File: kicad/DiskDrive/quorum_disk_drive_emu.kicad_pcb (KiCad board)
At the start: 2 copper layers, 185 x 115 mm, 89 parts, among them X1 CONN_28, X103 CONN_28, X104 CONN_28, X2 CONN_28, X3 FDD, X4 FDD POWER

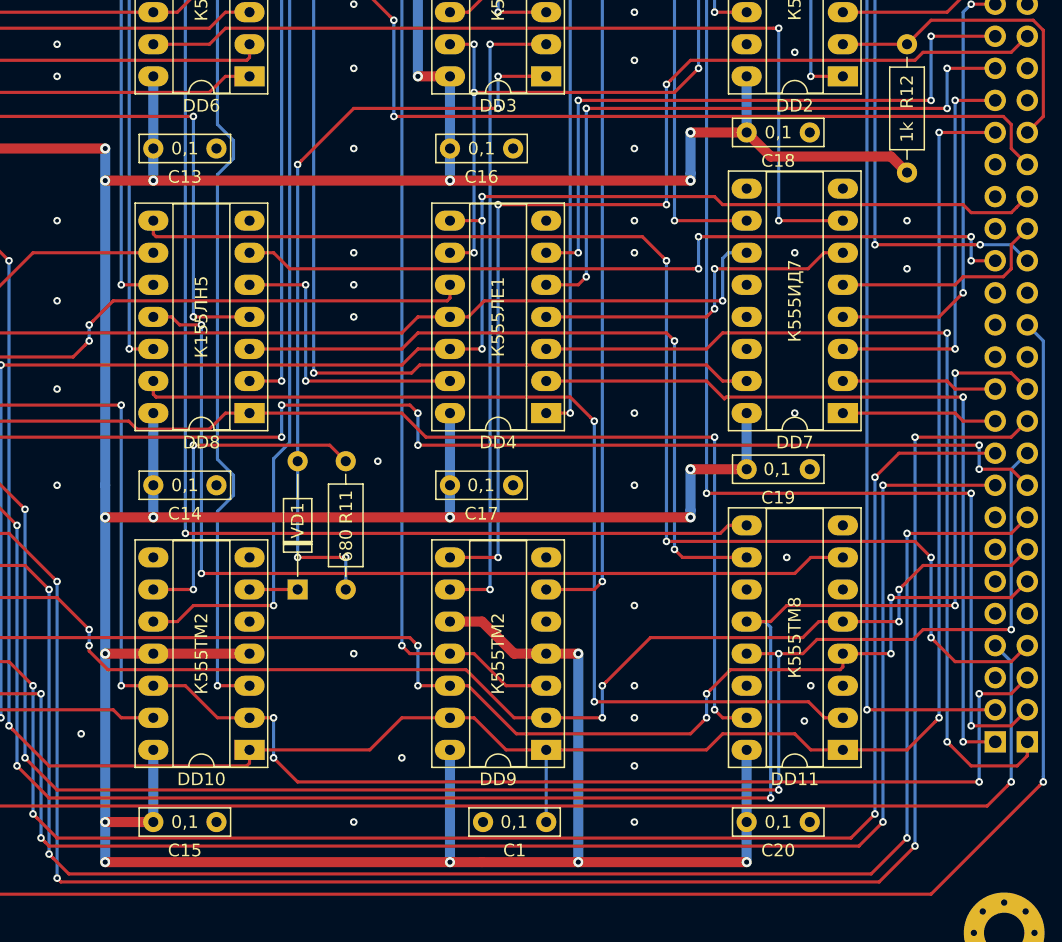
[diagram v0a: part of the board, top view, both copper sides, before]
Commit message: Обновлены УГО разъемов, исправлены множественные ошибки в схемах клавиатур
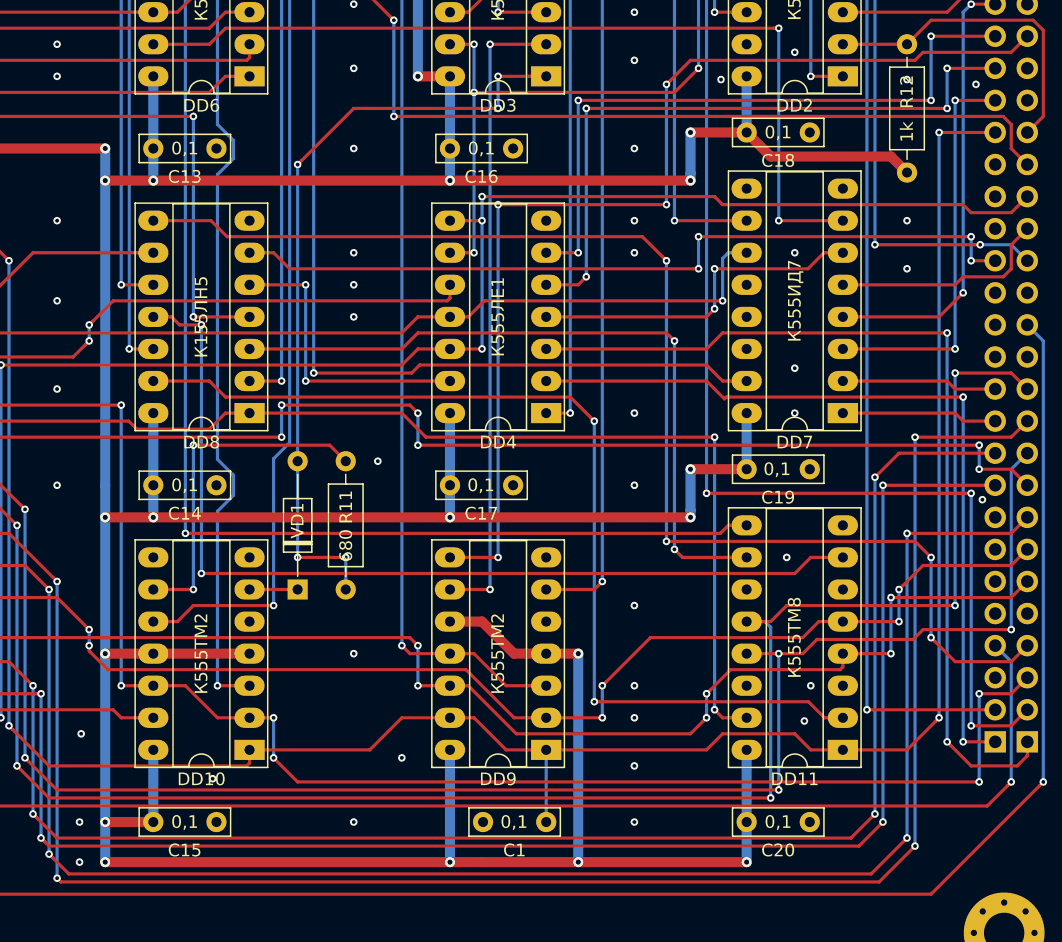
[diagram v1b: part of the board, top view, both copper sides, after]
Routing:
- net /~RAMCS: track 101.6 -> 100.9 mm
- net /DS0: track 79.3 -> 78.7 mm
- net GND: vias 73 -> 81
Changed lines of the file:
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@@
-(kicad_pcb (version 20171130) (host pcbnew 5.1.5+dfsg1-2)
+(kicad_pcb (version 20171130) (host pcbnew 5.1.5+dfsg1-2+b1)
   (general
     (thickness 1.6)
     (drawings 4)
-    (tracks 1337)
+    (tracks 1345)
     (zones 0)
     (modules 89)
@@
   (gr_line (start -140 255) (end 45 255) (layer Edge.Cuts) (width 0.1))
   (gr_line (start -140 140) (end -140 255) (layer Edge.Cuts) (width 0.1))
+  (via (at 38.274 215.693) (size 0.6) (drill 0.3) (layers F.Cu B.Cu) (net 1))
   (via (at 32.305 193.595) (size 0.6) (drill 0.3) (layers F.Cu B.Cu) (net 1))
   (via (at 32.305 197.405) (size 0.6) (drill 0.3) (layers F.Cu B.Cu) (net 1))
@@
   (via (at 22.78 174.545) (size 0.6) (drill 0.3) (layers F.Cu B.Cu) (net 1))
   (via (at 23.415 180.26) (size 0.6) (drill 0.3) (layers F.Cu B.Cu) (net 1))
+  (via (at 23.415 205.279) (size 0.6) (drill 0.3) (layers F.Cu B.Cu) (net 1))
+  (via (at 32.305 182.419) (size 0.6) (drill 0.3) (layers F.Cu B.Cu) (net 1))
+  (via (at 17.573 182.419) (size 0.6) (drill 0.3) (layers F.Cu B.Cu) (net 1))
+  (via (at 37.766 182.8) (size 0.6) (drill 0.3) (layers F.Cu B.Cu) (net 1))
+  (via (at -22.686 237.791) (size 0.6) (drill 0.3) (layers F.Cu B.Cu) (net 1))
+  (via (at -33.227 241.22) (size 0.6) (drill 0.3) (layers F.Cu B.Cu) (net 1))
+  (via (at -33.227 244.395) (size 0.6) (drill 0.3) (layers F.Cu B.Cu) (net 1))
   (segment (start -19.765 235.505) (end -10.24 235.505) (width 0.25) (layer F.Cu) (net 2))
   (segment (start -7.7 232.965) (end -3.89 232.965) (width 0.25) (layer F.Cu) (net 2))
@@
   (segment (start 25.775 232.965) (end 24.505 231.695) (width 0.25) (layer F.Cu) (net 45))
   (via (at 7.54 209.47) (size 0.6) (drill 0.3) (layers F.Cu B.Cu) (net 45))
-  (segment (start 5.635 207.565) (end 7.240001 209.170001) (width 0.25) (layer F.Cu) (net 45))
-  (segment (start -27.385 207.345) (end -27.165 207.565) (width 0.25) (layer F.Cu) (net 45))
   (segment (start 7.54 231.695) (end 7.54 209.47) (width 0.25) (layer B.Cu) (net 45))
-  (segment (start -27.385 206.295) (end -27.385 207.345) (width 0.25) (layer F.Cu) (net 45))
   (segment (start 7.240001 209.170001) (end 7.54 209.47) (width 0.25) (layer F.Cu) (net 45))
-  (segment (start -27.165 207.565) (end 5.635 207.565) (width 0.25) (layer F.Cu) (net 45))
+  (segment (start 5.635 207.565) (end 7.240001 209.170001) (width 0.25) (layer F.Cu) (net 45))
+  (segment (start -21.67 207.565) (end 5.635 207.565) (width 0.25) (layer F.Cu) (net 45))
+  (segment (start -22.94 206.295) (end -21.67 207.565) (width 0.25) (layer F.Cu) (net 45))
+  (segment (start -27.385 206.295) (end -22.94 206.295) (width 0.25) (layer F.Cu) (net 45))
   (via (at -29.29 203.755) (size 0.6) (drill 0.3) (layers F.Cu B.Cu) (net 46))
   (segment (start -27.385 203.755) (end -29.29 203.755) (width 0.25) (layer F.Cu) (net 46))
@@
   (segment (start -17.86 196.135) (end -16.589999 197.405001) (width 0.25) (layer F.Cu) (net 98))
   (via (at 13.255 218.995) (size 0.6) (drill 0.3) (layers F.Cu B.Cu) (net 99))
-  (segment (start 12.955001 196.470001) (end 13.255 196.77) (width 0.25) (layer F.Cu) (net 99))
   (segment (start 13.255 218.995) (end 13.255 196.77) (width 0.25) (layer B.Cu) (net 99))
-  (segment (start -27.385 194.645) (end -27.165 194.865) (width 0.25) (layer F.Cu) (net 99))
-  (segment (start -27.385 193.595) (end -27.385 194.645) (width 0.25) (layer F.Cu) (net 99))
-  (segment (start 11.35 194.865) (end 12.955001 196.470001) (width 0.25) (layer F.Cu) (net 99))
   (via (at 13.255 196.77) (size 0.6) (drill 0.3) (layers F.Cu B.Cu) (net 99))
-  (segment (start -27.165 194.865) (end 11.35 194.865) (width 0.25) (layer F.Cu) (net 99))
   (via (at 34.21 220.265) (size 0.6) (drill 0.3) (layers F.Cu B.Cu) (net 99))
   (segment (start 32.94 218.995) (end 34.21 220.265) (width 0.25) (layer F.Cu) (net 99))
@@
   (segment (start 34.21 220.265) (end 34.21 226.615) (width 0.25) (layer B.Cu) (net 99))
   (via (at 34.21 226.615) (size 0.6) (drill 0.3) (layers F.Cu B.Cu) (net 99))
+  (segment (start 12.955001 196.470001) (end 13.255 196.77) (width 0.25) (layer F.Cu) (net 99))
+  (segment (start 11.35 194.865) (end 12.955001 196.470001) (width 0.25) (layer F.Cu) (net 99))
+  (segment (start -22.813 193.595) (end -21.543 194.865) (width 0.25) (layer F.Cu) (net 99))
+  (segment (start -21.543 194.865) (end 11.35 194.865) (width 0.25) (layer F.Cu) (net 99))
+  (segment (start -27.385 193.595) (end -22.813 193.595) (width 0.25) (layer F.Cu) (net 99))
   (via (at 8.175 222.17) (size 0.6) (drill 0.3) (layers F.Cu B.Cu) (net 100))
   (segment (start 3.73 222.805) (end 7.54 222.805) (width 0.25) (layer F.Cu) (net 100))
